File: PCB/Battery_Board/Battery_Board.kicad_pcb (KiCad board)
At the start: 2 copper layers, 90 x 90 mm, 4 parts, among them J1 SE2-30

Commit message: edits from meeting
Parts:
- moved BT1 4.00 mm to (181.8, 63.0)
- moved BT2 4.00 mm to (181.8, 88.5)
- moved BT3 4.00 mm to (181.8, 114.2)
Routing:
- net VBUS: track 97.8 -> 96.2 mm
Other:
- board size 90 x 90 mm -> 90 x 85 mm
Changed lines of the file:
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@@
 			(unlocked yes)
 			(layer "F.SilkS")
+			(hide yes)
 			(effects
 				(font
@@
 		)
 		(fp_line
-			(start -45 4.500001)
-			(end -45 85)
+			(start -45 4.5)
+			(end -45 80.01)
 			(stroke
 				(width 0.05)
-				(type default)
+				(type solid)
 			)
 			(layer "Edge.Cuts")
 		)
 		(fp_line
-			(start -44 86)
-			(end 44 86)
+			(start -44 81)
+			(end 44 81)
 			(stroke
 				(width 0.05)
@@
 		(fp_line
 			(start 45 4.49)
-			(end 45 85)
+			(end 45 80)
 			(stroke
 				(width 0.05)
-				(type default)
+				(type solid)
 			)
 			(layer "Edge.Cuts")
@@
 		)
 		(fp_arc
-			(start -44 86)
-			(mid -44.707107 85.707107)
-			(end -45 85)
+			(start -44 81)
+			(mid -44.707107 80.707107)
+			(end -45 80)
 			(stroke
 				(width 0.05)
@@
 		)
 		(fp_arc
-			(start 45 85)
-			(mid 44.707107 85.707107)
-			(end 44 86)
+			(start 45 80)
+			(mid 44.707107 80.707107)
+			(end 44 81)
 			(stroke
 				(width 0.05)
@@
 		)
 		(fp_text user "TOP"
-			(at -44 85 0)
+			(at -44 80 0)
 			(unlocked yes)
 			(layer "F.SilkS")
@@
 		)
 		(fp_text user "BOTTOM"
-			(at -44 85 0)
+			(at -44 80 0)
 			(unlocked yes)
 			(layer "B.SilkS")
@@
 			(layer "Cmts.User")
 			(pts
+				(xy 178.13 42) (xy 256.87 42)
+			)
+			(height -10.5)
+			(orientation 0)
+			(format
+				(prefix "")
+				(suffix "")
+				(units 3)
+				(units_format 0)
+				(precision 4)
+				(suppress_zeroes yes)
+			)
+			(style
+				(thickness 0.1)
+				(arrow_length 1.27)
+				(text_position_mode 0)
+				(arrow_direction outward)
+				(extension_height 0.58642)
+				(extension_offset 0.5)
+				(keep_text_aligned yes)
+			)
+			(gr_text "78.74"
+				(at 217.5 30.4 0)
+				(layer "Cmts.User")
+				(effects
+					(font
+						(size 1 1)
+						(thickness 0.1)
+					)
+				)
+			)
+		)
+		(dimension
+			(type orthogonal)
+			(layer "Cmts.User")
+			(pts
 				(xy 256.87 42) (xy 256.87 49.49)
 			)
@@
 			(layer "Cmts.User")
 			(pts
-				(xy 172.5 132) (xy 262.5 132)
+				(xy 262.5 127.5) (xy 262.207107 49.5)
 			)
-			(height 12)
-			(orientation 0)
+			(height 11.5)
+			(orientation 1)
 			(format
 				(prefix "")
@@
 				(keep_text_aligned yes)
 			)
-			(gr_text "90"
-				(at 217.5 142.85 0)
+			(gr_text "78"
+				(at 272.85 88.5 90)
 				(layer "Cmts.User")
 				(effects
@@
 			(layer "Cmts.User")
 			(pts
-				(xy 178.13 42) (xy 256.87 42)
+				(xy 267.5 127.5) (xy 267.207107 42)
 			)
-			(height -10.5)
-			(orientation 0)
+			(height 11.5)
+			(orientation 1)
 			(format
 				(prefix "")
@@
 			)
 			(style
-				(thickness 0.1)
+				(thickness 0.05)
 				(arrow_length 1.27)
 				(text_position_mode 0)
@@
 				(keep_text_aligned yes)
 			)
-			(gr_text "78.74"
-				(at 217.5 30.4 0)
+			(gr_text "85.5"
+				(at 277.85 84.75 90)
 				(layer "Cmts.User")
 				(effects
 					(font
 						(size 1 1)
-						(thickness 0.1)
+						(thickness 0.15)
 					)
 				)
@@
 			(layer "Cmts.User")
 			(pts
-				(xy 262.5 132) (xy 262.5 49.49)
+				(xy 172.5 127) (xy 262.5 127)
 			)
-			(height 11.5)
-			(orientation 1)
+			(height 12)
+			(orientation 0)
 			(format
 				(prefix "")
@@
 				(keep_text_aligned yes)
 			)
-			(gr_text "82.51"
-				(at 272.85 90.745 90)
+			(gr_text "90"
+				(at 217.5 137.85 0)
 				(layer "Cmts.User")
 				(effects
@@
 		)
 		(group ""
-			(members "0576a331-9f76-401f-ac96-d302c2b2379b" "099aa479-7b72-4a4c-a769-8518bc94f07f"
-				"1f978678-9fc6-4bec-9ca9-02e1599cec2f" "27cee22b-b478-4347-aa44-11140595800f"
-				"29875613-e73a-495e-9083-c9885d887a25" "2a0c306a-fdfe-43d5-a334-9794d8d520a3"
-				"4700ff43-c1d3-4c62-86c6-1426cdb297bd" "572e2d59-fd76-4914-a222-ecfe9b0544c9"
-				"6bf05120-a336-436d-8543-32eb7675340c" "6d798e41-cb84-4aac-abf0-22e6f1867561"
-				"723e9221-29d5-4341-88ad-08831b8e28a3" "7f71f75a-72a5-4812-b113-32c8ab858674"
-				"833661ed-15f4-4b34-b7ac-0dae79ed6555" "886374e7-eb69-42c8-bf5a-29edd44aea2c"
-				"8c5bcbdd-1bc6-4fa8-9cfd-8305585a3a0f" "8ede6605-373b-4457-8394-add15065966f"
-				"8f926001-9687-45b1-af0e-f0e6804b1232" "9616212e-ddeb-464e-ba2a-f3652c605924"
-				"a6f6ed38-8c80-45d3-b3c7-c804da35cb93" "a7b35c75-fda6-4a59-b0b7-3dbb266fe900"
-				"adab6477-f7f5-4164-8f7b-e38af7eb5a59" "b5f7db92-ed44-4e38-bdac-5c0cba2ea7c7"
-				"ce6bccaa-8fed-41bf-aac4-a5a355f3a8b7" "d0f0d393-7671-4937-bf78-a173aa1db914"
-				"dc6bacf0-e5fd-4b17-ae37-7d0142fdcd1c" "dfc64a73-e850-4149-a8c4-79cb9051a176"
-				"e6e6bbec-4fa2-47b2-8fb0-a771e8328cb0" "e8f1f9bd-b0bc-410a-b6fe-93093eb8addd"
-				"f3149af5-1fe6-4d6f-bb96-aaf2cd4da463" "f68173f6-cd59-4c9e-98bc-a7722907d220"
-				"f922a95d-d4cd-4958-ba62-2a210f3c6677"
+			(members "01ceb4d7-95a9-4715-8b54-7b6caa1cadf4" "02076a63-9917-4e24-a663-0149b9bb5b17"
+				"02e9ad1f-8e94-436c-a87a-4f6fb173b84c" "08a04171-eadc-4275-aa42-c85b388e8773"
+				"110bedc4-5d3d-4ae5-b3bc-c95eb5f47476" "1802cfd3-1e43-46db-acbb-099de4b3b90c"
+				"2227c4c2-d2ef-4f95-b9f6-790a28e5d98c" "2abe32f9-517c-4c12-a889-542dc000e172"
+				"2cb27459-94ce-4522-972a-630bd1ebb40d" "38a1d972-df17-4b4f-a38d-c216954af38a"
+				"46406e21-b3fa-4dd2-8b17-17e968e4e5c5" "5ca96600-b42e-42dd-b97f-97355b204386"
+				"65c7c494-3c50-48c8-92cb-db0b18618085" "6c723505-714b-4f0f-a105-da710104e54f"
+				"70d2f12b-4495-4352-873b-5883c26ae163" "7a911669-cc2a-41d0-99fd-a1e85cbb01c7"
+				"7c43dd13-a671-45a3-9476-cfae4376c597" "891dffce-6605-4464-98c8-2f31cfdd79fd"
+				"89aada95-2ee9-4c5b-9339-a7812df6a316" "940b537b-df54-4350-bb10-e3a75d4bcdd0"
+				"9a8d925c-1dfc-47a4-873d-8d99bf2f9ae6" "9d6a41c1-f18f-436b-833d-b316eedfdd30"
+				"9d96d457-b2b6-47cc-a804-3e302d1c7f6d" "ae9afbf3-05ef-4faf-96bb-8ff14be817ec"
+				"be1c2783-6d61-4ae9-bac6-a30863c695ad" "bea0b7e5-06eb-4680-ae37-578f333a01d8"
+				"c8f57011-5123-477d-ae20-199cb2d90c9f" "d5551b4f-07b9-49e6-ac4c-95ea77f40f64"
+				"f1743469-f647-49cf-8a1c-7979b37cce3b" "f184c074-2fca-4ee6-b85a-682eb8421d94"
+				"fae93057-a3b3-4aa7-93e1-f8272b9e41f8"
 			)
 		)
 		(group ""
-			(members "05cd00b3-f595-4347-87c7-70b54c5663ee" "07c7a2e0-46ce-4c1c-90d0-b701c67f37f3"
-				"0e79a1ce-c1ad-4d48-8972-d496fbdfae5b" "1a5604f0-b87b-42cb-83b4-87db2195a045"
-				"212fc3bd-7cea-4ebc-a4ae-d3dc07d95503" "cec5d429-1663-4ff6-ae85-c53572afcdeb"
+			(members "05571765-961c-47ef-875d-9e8820501feb" "0923ca63-275c-462e-ae7b-37d8e9938db9"
+				"2d3d227e-22c0-4674-99fb-4ce77206abb8" "3299c99c-c4bb-4d60-9ffd-9c8dc9cd9578"
+				"6b79917f-da90-47f8-860a-b910efcf7c59" "8acd7ca3-e90a-4b1c-82ba-3497edefcdd9"
 			)
 		)
@@
 	(footprint "Battery:BatteryHolder_MPD_BK-18650-PC2"
 		(layer "F.Cu")
-		(at 181.751029 92.5)
+		(at 181.751029 88.5)
 		(descr "Battery holder, MPD BK-18650, battery type 1x18650, https://www.batteryholders.com/uploads/parts/BK-18650-PC2/datasheets/BK-18650-PC2-datasheet.pdf, generated with kicad-footprint-generator StandardBox_generator.py")
 		(tags "horizontal single")
@@
 	(footprint "Battery:BatteryHolder_MPD_BK-18650-PC2"
 		(layer "F.Cu")
-		(at 181.751029 67)
+		(at 181.751029 63)
 		(descr "Battery holder, MPD BK-18650, battery type 1x18650, https://www.batteryholders.com/uploads/parts/BK-18650-PC2/datasheets/BK-18650-PC2-datasheet.pdf, generated with kicad-footprint-generator StandardBox_generator.py")
 		(tags "horizontal single")
@@
 	(footprint "Battery:BatteryHolder_MPD_BK-18650-PC2"
 		(layer "F.Cu")
-		(at 181.751029 118.21)
+		(at 181.751029 114.21)
 		(descr "Battery holder, MPD BK-18650, battery type 1x18650, https://www.batteryholders.com/uploads/parts/BK-18650-PC2/datasheets/BK-18650-PC2-datasheet.pdf, generated with kicad-footprint-generator StandardBox_generator.py")
 		(tags "horizontal single")
@@
 	)
 	(segment
+		(start 185.751029 63)
+		(end 181.751029 63)
+		(width 0.75)
+		(layer "F.Cu")
+		(net 1)
+	)
+	(segment
 		(start 246.17 51.67)
 		(end 246.67 51.17)
@@
 	)
 	(segment
-		(start 181.751029 67)
-		(end 193.751029 55)
+		(start 244.67 53.17)
+		(end 245.17 52.67)
 		(width 0.75)
 		(layer "F.Cu")
@@
 	)
 	(segment
-		(start 244.67 53.17)
-		(end 245.17 52.67)
+		(start 193.751029 55)
+		(end 185.751029 63)
 		(width 0.75)
 		(layer "F.Cu")
@@
 	)
 	(segment
-		(start 253.251029 79.75)
-		(end 183.001029 79.75)
+		(start 253.251029 75.75)
+		(end 183.001029 75.75)
 		(width 0.75)
 		(layer "F.Cu")
@@
 	)
 	(segment
-		(start 254.651029 78.35)
-		(end 253.251029 79.75)
+		(start 254.651029 74.35)
+		(end 253.251029 75.75)
 		(width 0.75)
 		(layer "F.Cu")
@@
 	)
 	(segment
-		(start 181.751029 81)
-		(end 181.751029 92.5)
+		(start 181.751029 77)
+		(end 181.751029 88.5)
 		(width 0.75)
 		(layer "F.Cu")
@@
 	)
 	(segment
-		(start 254.651029 67)
-		(end 254.651029 78.35)
+		(start 254.651029 63)
+		(end 254.651029 74.35)
 		(width 0.75)
 		(layer "F.Cu")
@@
 	)
 	(segment
-		(start 183.001029 79.75)
-		(end 181.751029 81)
+		(start 183.001029 75.75)
+		(end 181.751029 77)
 		(width 0.75)
 		(layer "F.Cu")
@@
 	)
 	(segment
-		(start 254.651029 92.5)
-		(end 254.651029 103.85)
+		(start 254.651029 88.5)
+		(end 254.651029 99.85)
 		(width 0.75)
 		(layer "F.Cu")
@@
 	)
 	(segment
-		(start 181.751029 107)
-		(end 181.751029 118.21)
+		(start 181.751029 103)
+		(end 181.751029 114.21)
 		(width 0.75)
 		(layer "F.Cu")
@@
 	)
 	(segment
-		(start 253.001029 105.5)
-		(end 183.251029 105.5)
+		(start 253.001029 101.5)
+		(end 183.251029 101.5)
 		(width 0.75)
 		(layer "F.Cu")
@@
 	)
 	(segment
-		(start 183.251029 105.5)
-		(end 181.751029 107)
+		(start 183.251029 101.5)
+		(end 181.751029 103)
 		(width 0.75)
 		(layer "F.Cu")
@@
 	)
 	(segment
-		(start 254.651029 103.85)
-		(end 253.001029 105.5)
+		(start 254.651029 99.85)
+		(end 253.001029 101.5)
 		(width 0.75)
 		(layer "F.Cu")

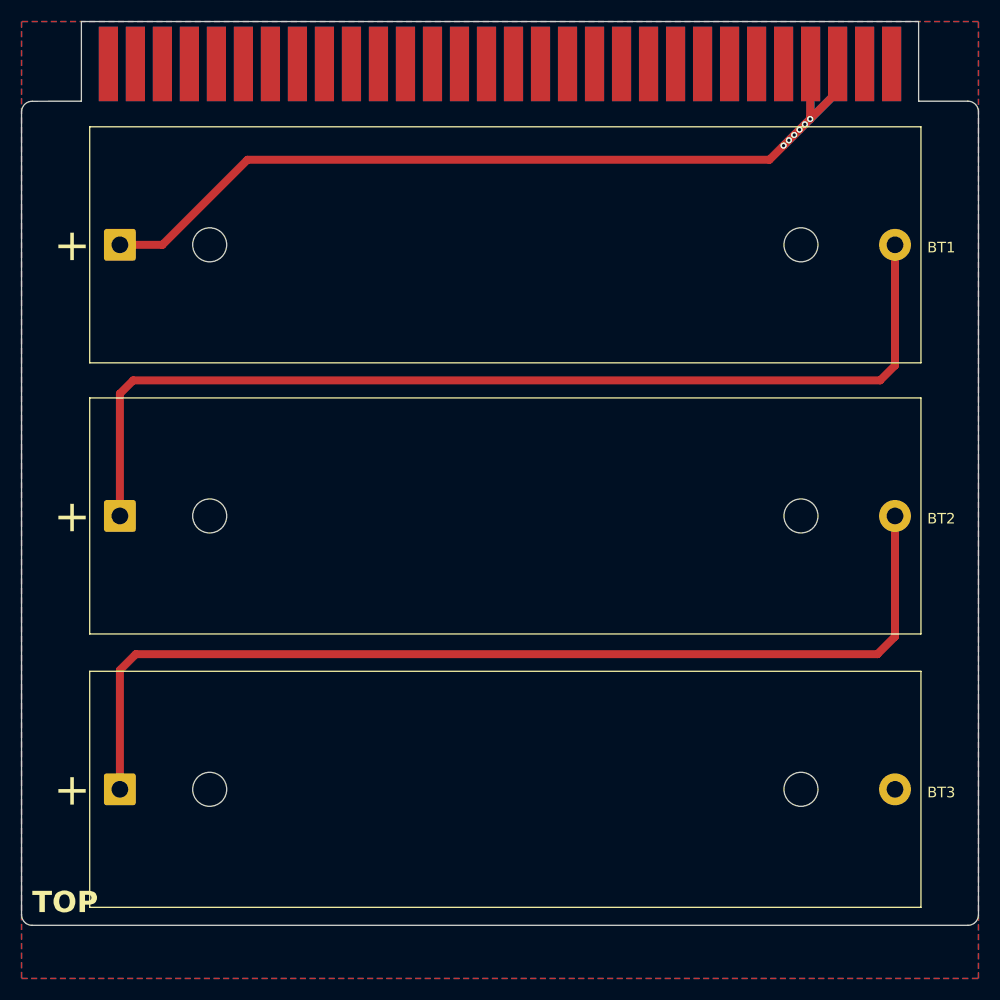
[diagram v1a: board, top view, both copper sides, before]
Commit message: updated board footprint and rerouted
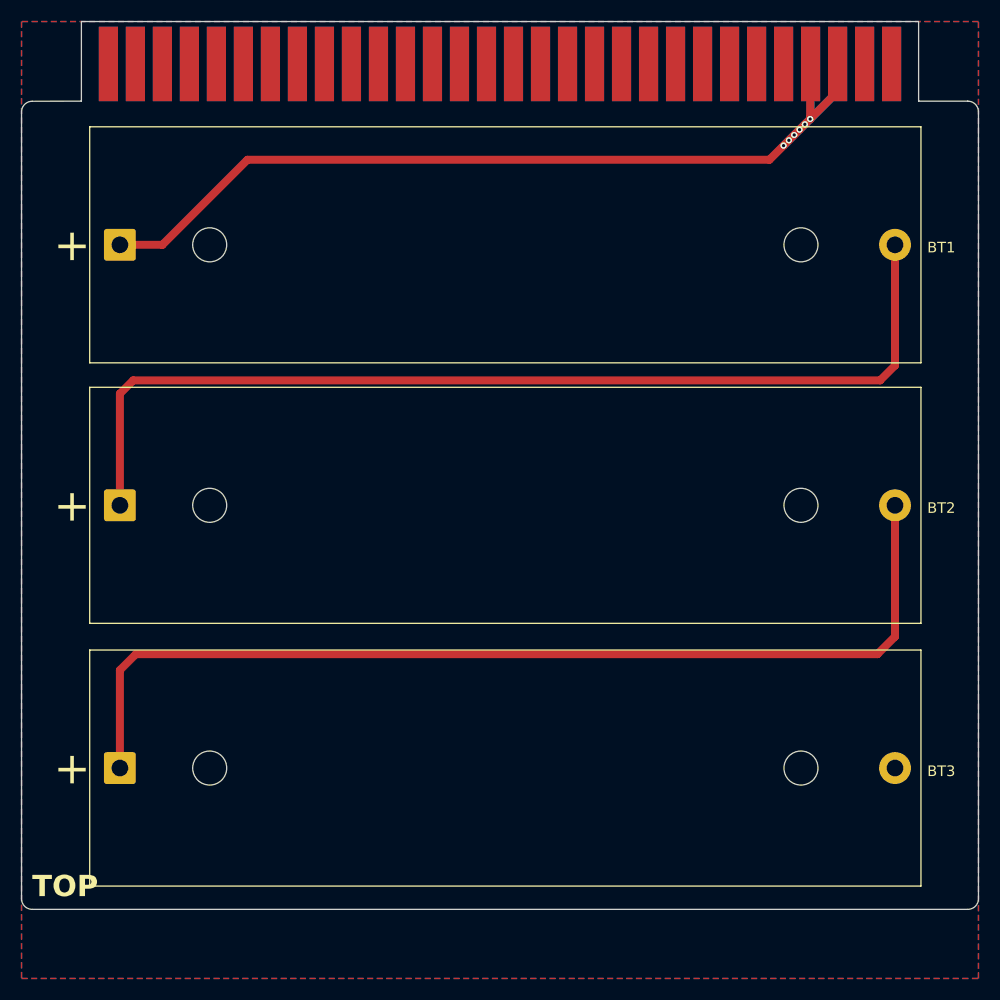
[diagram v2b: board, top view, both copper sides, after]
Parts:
- moved BT3 2.00 mm to (181.8, 112.2)
- moved BT2 1.00 mm to (181.8, 87.5)
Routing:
- net Net-(BT2--): track 96.8 -> 94.8 mm
- net Net-(BT1--): track 96.8 -> 95.8 mm
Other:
- board size 90 x 85 mm -> 90 x 83.5 mm
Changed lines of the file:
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@@
 		(fp_line
 			(start -45 4.5)
-			(end -45 80.01)
+			(end -45 78.5)
 			(stroke
 				(width 0.05)
@@
 		)
 		(fp_line
-			(start -44 81)
-			(end 44 81)
+			(start -44 79.5)
+			(end 44 79.5)
 			(stroke
 				(width 0.05)
@@
 		(fp_line
 			(start 45 4.49)
-			(end 45 80)
+			(end 45 78.5)
 			(stroke
 				(width 0.05)
@@
 		)
 		(fp_arc
-			(start -44 81)
-			(mid -44.707107 80.707107)
-			(end -45 80)
+			(start -44 79.5)
+			(mid -44.707107 79.207107)
+			(end -45 78.5)
 			(stroke
 				(width 0.05)
@@
 		)
 		(fp_arc
-			(start 45 80)
-			(mid 44.707107 80.707107)
-			(end 44 81)
+			(start 45 78.5)
+			(mid 44.707107 79.207107)
+			(end 44 79.5)
 			(stroke
 				(width 0.05)
@@
 		)
 		(fp_text user "TOP"
-			(at -44 80 0)
+			(at -44 78.5 0)
 			(unlocked yes)
 			(layer "F.SilkS")
@@
 		)
 		(fp_text user "BOTTOM"
-			(at -44 80 0)
+			(at -44 78.5 0)
 			(unlocked yes)
 			(layer "B.SilkS")
@@
 			(layer "Cmts.User")
 			(pts
-				(xy 256.87 42) (xy 256.87 49.49)
+				(xy 262.5 125.5) (xy 262.207107 49.5)
 			)
-			(height 9.63)
+			(height 11.5)
 			(orientation 1)
 			(format
@@
 			)
 			(style
-				(thickness 0.1)
+				(thickness 0.05)
 				(arrow_length 1.27)
 				(text_position_mode 0)
@@
 				(keep_text_aligned yes)
 			)
-			(gr_text "7.49"
-				(at 265.4 45.745 90)
+			(gr_text "76"
+				(at 272.85 87.5 90)
 				(layer "Cmts.User")
 				(effects
 					(font
 						(size 1 1)
-						(thickness 0.1)
+						(thickness 0.15)
 					)
 				)
@@
 			(layer "Cmts.User")
 			(pts
-				(xy 262.5 127.5) (xy 262.207107 49.5)
+				(xy 172.5 125.5) (xy 262.5 125.5)
 			)
-			(height 11.5)
-			(orientation 1)
+			(height 12)
+			(orientation 0)
 			(format
 				(prefix "")
@@
 				(keep_text_aligned yes)
 			)
-			(gr_text "78"
-				(at 272.85 88.5 90)
+			(gr_text "90"
+				(at 217.5 136.35 0)
 				(layer "Cmts.User")
 				(effects
@@
 			(layer "Cmts.User")
 			(pts
-				(xy 267.5 127.5) (xy 267.207107 42)
+				(xy 256.87 42) (xy 256.87 49.49)
 			)
-			(height 11.5)
+			(height 9.63)
 			(orientation 1)
 			(format
@@
 			)
 			(style
-				(thickness 0.05)
+				(thickness 0.1)
 				(arrow_length 1.27)
 				(text_position_mode 0)
@@
 				(keep_text_aligned yes)
 			)
-			(gr_text "85.5"
-				(at 277.85 84.75 90)
+			(gr_text "7.49"
+				(at 265.4 45.745 90)
 				(layer "Cmts.User")
 				(effects
 					(font
 						(size 1 1)
-						(thickness 0.15)
+						(thickness 0.1)
 					)
 				)
@@
 			(layer "Cmts.User")
 			(pts
-				(xy 172.5 127) (xy 262.5 127)
+				(xy 267.5 125.5) (xy 267.207107 42)
 			)
-			(height 12)
-			(orientation 0)
+			(height 11.5)
+			(orientation 1)
 			(format
 				(prefix "")
@@
 				(keep_text_aligned yes)
 			)
-			(gr_text "90"
-				(at 217.5 137.85 0)
+			(gr_text "83.5"
+				(at 277.85 83.75 90)
 				(layer "Cmts.User")
 				(effects
@@
 		)
 		(group ""
-			(members "01ceb4d7-95a9-4715-8b54-7b6caa1cadf4" "02076a63-9917-4e24-a663-0149b9bb5b17"
-				"02e9ad1f-8e94-436c-a87a-4f6fb173b84c" "08a04171-eadc-4275-aa42-c85b388e8773"
-				"110bedc4-5d3d-4ae5-b3bc-c95eb5f47476" "1802cfd3-1e43-46db-acbb-099de4b3b90c"
-				"2227c4c2-d2ef-4f95-b9f6-790a28e5d98c" "2abe32f9-517c-4c12-a889-542dc000e172"
-				"2cb27459-94ce-4522-972a-630bd1ebb40d" "38a1d972-df17-4b4f-a38d-c216954af38a"
-				"46406e21-b3fa-4dd2-8b17-17e968e4e5c5" "5ca96600-b42e-42dd-b97f-97355b204386"
-				"65c7c494-3c50-48c8-92cb-db0b18618085" "6c723505-714b-4f0f-a105-da710104e54f"
-				"70d2f12b-4495-4352-873b-5883c26ae163" "7a911669-cc2a-41d0-99fd-a1e85cbb01c7"
-				"7c43dd13-a671-45a3-9476-cfae4376c597" "891dffce-6605-4464-98c8-2f31cfdd79fd"
-				"89aada95-2ee9-4c5b-9339-a7812df6a316" "940b537b-df54-4350-bb10-e3a75d4bcdd0"
-				"9a8d925c-1dfc-47a4-873d-8d99bf2f9ae6" "9d6a41c1-f18f-436b-833d-b316eedfdd30"
-				"9d96d457-b2b6-47cc-a804-3e302d1c7f6d" "ae9afbf3-05ef-4faf-96bb-8ff14be817ec"
-				"be1c2783-6d61-4ae9-bac6-a30863c695ad" "bea0b7e5-06eb-4680-ae37-578f333a01d8"
-				"c8f57011-5123-477d-ae20-199cb2d90c9f" "d5551b4f-07b9-49e6-ac4c-95ea77f40f64"
-				"f1743469-f647-49cf-8a1c-7979b37cce3b" "f184c074-2fca-4ee6-b85a-682eb8421d94"
-				"fae93057-a3b3-4aa7-93e1-f8272b9e41f8"
+			(members "0564de8e-eea9-40d3-a141-6267f791b5d6" "056a5dbe-30c0-49f1-a35d-70aae5f27bb4"
+				"1e7501eb-41fb-4ff5-8459-e773d91fc00e" "24105261-4018-40b7-b64b-5e396355e80e"
+				"584f1d91-5d84-4daf-9a9e-79f200a5497e" "702f11bd-f4b5-4cb6-b3a5-6c11e91a7121"
+				"758f0b23-85d6-4ec2-8bd7-6724d2307118" "78a2704b-38e2-4c9e-957c-8d38a52391dd"
+				"7916fdb4-789d-42b4-854d-bb09181874b8" "7e0035ce-bce7-4bc9-92da-252c7b003c46"
+				"8300ee87-e112-48b9-8e5c-f78deb9c65ce" "a8c0ffec-3117-41d9-85af-6fd4d47595bb"
+				"ac639a2b-b26f-48ba-b748-5cbb83c2947f" "b42605d9-6db3-4b03-b6f8-cd1e3365082e"
+				"b7a51747-fd4c-47f3-bb9a-31300fab9f90" "b917dc42-262c-4f73-af76-3a597d229325"
+				"bb410d53-8e7e-412d-bc21-1b9d96235c94" "bcaf50b7-7c98-4543-b0b7-10901923facd"
+				"bd5d97aa-78bd-4183-b268-d7073a29b86f" "c62e2c1d-d431-4e88-a01b-844c92ed0a57"
+				"c7cbe829-bed6-48b4-aa28-4e7e962f20c7" "ce26ebfe-7fba-4347-b215-be9f8c491c1c"
+				"cfd37bd8-d661-4832-82dc-98dde60630c3" "cfda4547-11d3-4880-aac9-6fd193554eb0"
+				"dbf9cce0-f556-49c5-a042-06303066692a" "ddd54e6c-c0b9-47e7-80c8-fe6d16000582"
+				"e4094b18-037d-42a1-ab01-47b054e8cbe3" "e6a45ab1-c733-4487-a319-47f6960a1cc6"
+				"e73ce176-ce9f-413b-9d4e-7a9753a2fcea" "eb77da85-d583-4e06-867b-c229833a080b"
+				"f7bf6b02-2cab-4b97-88ea-81f675b3b55b"
 			)
 		)
 		(group ""
-			(members "05571765-961c-47ef-875d-9e8820501feb" "0923ca63-275c-462e-ae7b-37d8e9938db9"
-				"2d3d227e-22c0-4674-99fb-4ce77206abb8" "3299c99c-c4bb-4d60-9ffd-9c8dc9cd9578"
-				"6b79917f-da90-47f8-860a-b910efcf7c59" "8acd7ca3-e90a-4b1c-82ba-3497edefcdd9"
+			(members "0801642a-1270-46be-bab8-dabf82b5c0e0" "5d1d4640-46b2-4058-98ae-abcf43560dad"
+				"74b86733-80f4-41e8-988d-7cd56037a90d" "7adacb92-2d08-4ee0-8a80-204fbd16e221"
+				"bac7c81d-55c9-48fc-8349-61006f4e86ad" "f2b25bc5-5ec3-49b7-84c6-a1c5e476af28"
 			)
 		)
@@
 	(footprint "Battery:BatteryHolder_MPD_BK-18650-PC2"
 		(layer "F.Cu")
-		(at 181.751029 88.5)
+		(at 181.751029 87.5)
 		(descr "Battery holder, MPD BK-18650, battery type 1x18650, https://www.batteryholders.com/uploads/parts/BK-18650-PC2/datasheets/BK-18650-PC2-datasheet.pdf, generated with kicad-footprint-generator StandardBox_generator.py")
 		(tags "horizontal single")
@@
 	(footprint "Battery:BatteryHolder_MPD_BK-18650-PC2"
 		(layer "F.Cu")
-		(at 181.751029 114.21)
+		(at 181.751029 112.21)
 		(descr "Battery holder, MPD BK-18650, battery type 1x18650, https://www.batteryholders.com/uploads/parts/BK-18650-PC2/datasheets/BK-18650-PC2-datasheet.pdf, generated with kicad-footprint-generator StandardBox_generator.py")
 		(tags "horizontal single")
@@
 	)
 	(segment
-		(start 181.751029 77)
-		(end 181.751029 88.5)
+		(start 254.651029 63)
+		(end 254.651029 74.35)
 		(width 0.75)
 		(layer "F.Cu")
@@
 	)
 	(segment
-		(start 254.651029 63)
-		(end 254.651029 74.35)
+		(start 181.751029 77)
+		(end 181.751029 87.5)
 		(width 0.75)
 		(layer "F.Cu")
@@
 	(segment
 		(start 181.751029 103)
-		(end 181.751029 114.21)
+		(end 181.751029 112.21)
 		(width 0.75)
 		(layer "F.Cu")
